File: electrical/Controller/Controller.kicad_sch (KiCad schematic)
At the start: 49 parts, among them J1 USB4105-GF-A, J2 UART, J3 SWD, J4 TC2030-NL, J5 I2C, SW1 SYS, U1 USBLC6-2P6, U2 LP5912-3.3DRV, U3 W25Q16JVUXIQ, U4 RP2040, U5 ABPMRRV001PD2A3, Y1 ABM8-272-T3

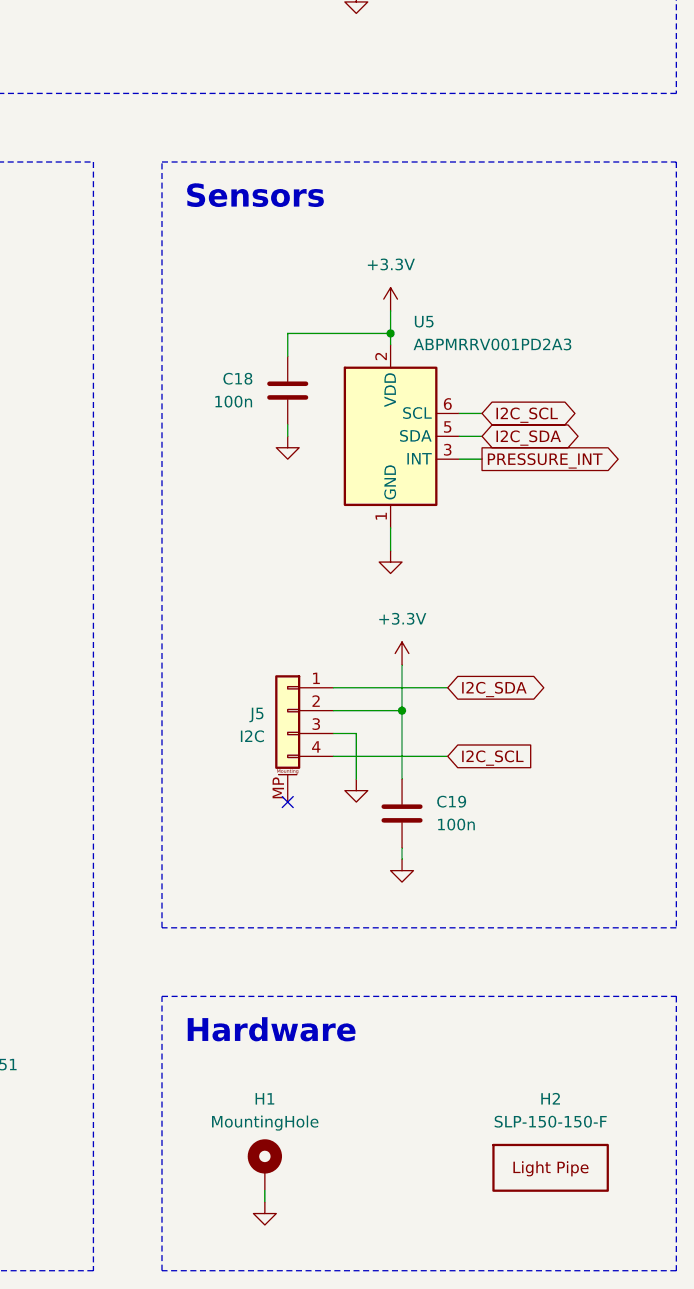
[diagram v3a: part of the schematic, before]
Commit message: Use 5-pin connector for I2C
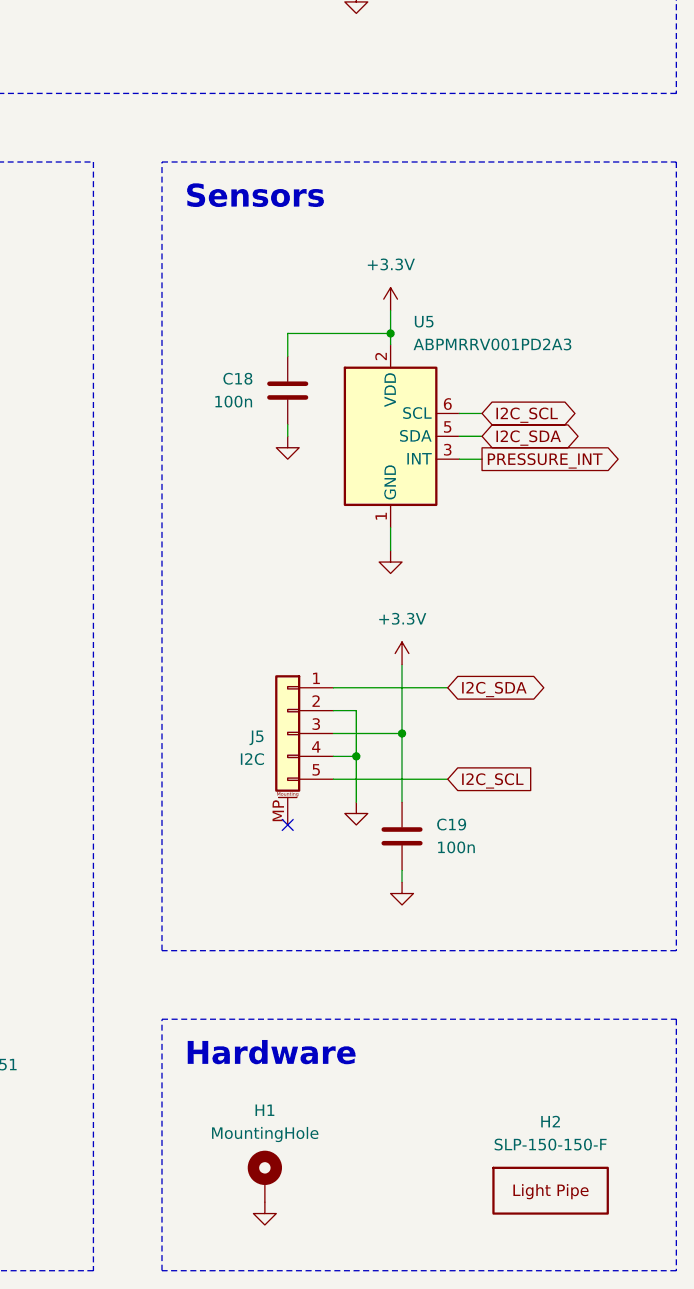
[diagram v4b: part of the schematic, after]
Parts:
- J5: footprint Connector_Molex:Molex_PicoBlade_53261-0471_1x04-1MP_P1.25mm_Horizontal -> Connector_Molex:Molex_PicoBlade_53261-0571_1x05-1MP_P1.25mm_Horizontal; symbol Connector_Generic_MountingPin:Conn_01x04_MountingPin -> Connector_Generic_MountingPin:Conn_01x05_MountingPin; LCSC C5119769 -> C392176
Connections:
- net +3.3V: now also J5.3 (Pin_3); no longer J5.2 (Pin_2)
- net GND: now also J5.2 (Pin_2), J5.4 (Pin_4); no longer J5.3 (Pin_3)
- net I2C_SCL: now also J5.5 (Pin_5); no longer J5.4 (Pin_4)
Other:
- moved on the sheet: C19, H1, H2
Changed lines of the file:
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@@
 	)
 	(rectangle
-		(start 331.47 193.04)
+		(start 331.47 195.58)
 		(end 388.62 223.52)
 		(stroke
@@
 	(rectangle
 		(start 331.47 100.33)
-		(end 388.62 185.42)
+		(end 388.62 187.96)
 		(stroke
 			(width 0)
@@
 	(text "Hardware"
 		(exclude_from_sim no)
-		(at 334.01 195.58 0)
+		(at 334.01 198.12 0)
 		(effects
 			(font
@@
 	)
 	(junction
+		(at 353.06 166.37)
+		(diameter 0)
+		(color 0 0 0 0)
+	)
+	(junction
 		(at 78.74 158.75)
 		(diameter 0)
@@
 	)
 	(junction
-		(at 358.14 161.29)
+		(at 358.14 163.83)
 		(diameter 0)
 		(color 0 0 0 0)
@@
 	)
 	(no_connect
-		(at 345.44 171.45)
+		(at 345.44 173.99)
 	)
 	(no_connect
@@
 	(wire
 		(pts
+			(xy 353.06 161.29) (xy 353.06 166.37)
+		)
+		(stroke
+			(width 0)
+			(type default)
+		)
+	)
+	(wire
+		(pts
 			(xy 88.9 152.4) (xy 91.44 152.4)
 		)
@@
 	(wire
 		(pts
-			(xy 350.52 166.37) (xy 363.22 166.37)
+			(xy 350.52 168.91) (xy 363.22 168.91)
 		)
 		(stroke
@@
 	(wire
 		(pts
-			(xy 353.06 163.83) (xy 353.06 168.91)
+			(xy 353.06 166.37) (xy 353.06 171.45)
 		)
 		(stroke
@@
 	(wire
 		(pts
-			(xy 358.14 168.91) (xy 358.14 161.29)
+			(xy 358.14 171.45) (xy 358.14 163.83)
 		)
 		(stroke
@@
 	(wire
 		(pts
-			(xy 350.52 163.83) (xy 353.06 163.83)
+			(xy 350.52 166.37) (xy 353.06 166.37)
 		)
 		(stroke
@@
 	(wire
 		(pts
-			(xy 358.14 161.29) (xy 358.14 156.21)
+			(xy 358.14 163.83) (xy 358.14 156.21)
 		)
 		(stroke
@@
 	(wire
 		(pts
-			(xy 350.52 161.29) (xy 358.14 161.29)
+			(xy 350.52 163.83) (xy 358.14 163.83)
 		)
 		(stroke
@@
 	(wire
 		(pts
-			(xy 77.47 67.31) (xy 77.47 69.85)
+			(xy 350.52 161.29) (xy 353.06 161.29)
 		)
 		(stroke
@@
 	(wire
 		(pts
-			(xy 264.16 69.85) (xy 264.16 72.39)
+			(xy 77.47 67.31) (xy 77.47 69.85)
 		)
 		(stroke
@@
 	(wire
 		(pts
-			(xy 342.9 215.9) (xy 342.9 214.63)
+			(xy 264.16 69.85) (xy 264.16 72.39)
 		)
 		(stroke
@@
 	(wire
 		(pts
-			(xy 358.14 177.8) (xy 358.14 176.53)
+			(xy 358.14 180.34) (xy 358.14 179.07)
 		)
 		(stroke
@@
 	(global_label "I2C_SCL"
 		(shape input)
-		(at 363.22 166.37 0)
+		(at 363.22 168.91 0)
 		(fields_autoplaced yes)
 		(effects
@@
 		)
 		(property "Intersheetrefs" "${INTERSHEET_REFS}"
-			(at 373.7647 166.37 0)
+			(at 373.7647 168.91 0)
 			(effects
 				(font
@@
 	(symbol
 		(lib_id "power:GND")
-		(at 358.14 177.8 0)
+		(at 358.14 180.34 0)
 		(unit 1)
 		(exclude_from_sim no)
@@
 		(fields_autoplaced yes)
 		(property "Reference" "#PWR0147"
-			(at 358.14 184.15 0)
+			(at 358.14 186.69 0)
 			(effects
 				(font
@@
 		)
 		(property "Value" "GND"
-			(at 358.14 182.88 0)
+			(at 358.14 185.42 0)
 			(effects
 				(font
@@
 		)
 		(property "Footprint" ""
-			(at 358.14 177.8 0)
+			(at 358.14 180.34 0)
 			(effects
 				(font
@@
 		)
 		(property "Datasheet" ""
-			(at 358.14 177.8 0)
+			(at 358.14 180.34 0)
 			(effects
 				(font
@@
 		)
 		(property "Description" "Power symbol creates a global label with name \"GND\" , ground"
-			(at 358.14 177.8 0)
+			(at 358.14 180.34 0)
 			(effects
 				(font
@@
 	(symbol
 		(lib_id "Device:C")
-		(at 358.14 172.72 0)
+		(at 358.14 175.26 0)
 		(unit 1)
 		(exclude_from_sim no)
@@
 		(dnp no)
 		(property "Reference" "C19"
-			(at 361.95 171.4499 0)
+			(at 361.95 173.9899 0)
 			(effects
 				(font
@@
 		)
 		(property "Value" "100n"
-			(at 361.95 173.9899 0)
+			(at 361.95 176.5299 0)
 			(effects
 				(font
@@
 		)
 		(property "Footprint" "Capacitor_SMD:C_0402_1005Metric"
-			(at 359.1052 176.53 0)
+			(at 359.1052 179.07 0)
 			(effects
 				(font
@@
 		)
 		(property "Datasheet" "~"
-			(at 358.14 172.72 0)
+			(at 358.14 175.26 0)
 			(effects
 				(font
@@
 		)
 		(property "Description" "Unpolarized capacitor"
-			(at 358.14 172.72 0)
+			(at 358.14 175.26 0)
 			(effects
 				(font
@@
 		)
 		(property "LCSC" "C1525"
-			(at 358.14 172.72 0)
+			(at 358.14 175.26 0)
 			(effects
 				(font
@@
 	)
 	(symbol
-		(lib_id "Connector_Generic_MountingPin:Conn_01x04_MountingPin")
-		(at 345.44 161.29 0)
+		(lib_id "Connector_Generic_MountingPin:Conn_01x05_MountingPin")
+		(at 345.44 163.83 0)
 		(mirror y)
 		(unit 1)
@@
 		(dnp no)
 		(property "Reference" "J5"
-			(at 342.9 161.6455 0)
+			(at 342.9 164.1855 0)
 			(effects
 				(font
@@
 		)
 		(property "Value" "I2C"
-			(at 342.9 164.1855 0)
+			(at 342.9 166.7255 0)
 			(effects
 				(font
@@
 			)
 		)
-		(property "Footprint" "Connector_Molex:Molex_PicoBlade_53261-0471_1x04-1MP_P1.25mm_Horizontal"
-			(at 345.44 161.29 0)
+		(property "Footprint" "Connector_Molex:Molex_PicoBlade_53261-0571_1x05-1MP_P1.25mm_Horizontal"
+			(at 345.44 163.83 0)
 			(effects
 				(font
@@
 			)
 		)
-		(property "Datasheet" "https://www.jst-mfg.com/product/pdf/eng/eSH.pdf"
-			(at 345.44 161.29 0)
+		(property "Datasheet" "https://www.molex.com/content/dam/molex/molex-dot-com/products/automated/en-us/salesdrawingpdf/532/53261/532610571_sd.pdf?inline"
+			(at 345.44 163.83 0)
 			(effects
 				(font
@@
 			)
 		)
-		(property "Description" "Molex 0532610471"
-			(at 345.44 161.29 0)
+		(property "Description" "Molex 0532610571"
+			(at 345.44 163.83 0)
 			(effects
 				(font
@@
 			)
 		)
-		(property "LCSC" "C5119769"
-			(at 345.44 161.29 0)
+		(property "LCSC" "C392176"
+			(at 345.44 163.83 0)
 			(effects
 				(font
@@
 		(pin "4"
 		)
+		(pin "5"
+		)
 		(instances
 			(project ""
@@
 	(symbol
 		(lib_id "power:GND")
-		(at 353.06 168.91 0)
+		(at 353.06 171.45 0)
 		(mirror y)
 		(unit 1)
@@
 		(fields_autoplaced yes)
 		(property "Reference" "#PWR0102"
-			(at 353.06 175.26 0)
+			(at 353.06 177.8 0)
 			(effects
 				(font
@@
 		)
 		(property "Value" "GND"
-			(at 353.06 173.99 0)
+			(at 353.06 176.53 0)
 			(effects
 				(font
@@
 		)
 		(property "Footprint" ""
-			(at 353.06 168.91 0)
+			(at 353.06 171.45 0)
 			(effects
 				(font
@@
 		)
 		(property "Datasheet" ""
-			(at 353.06 168.91 0)
+			(at 353.06 171.45 0)
 			(effects
 				(font
@@
 		)
 		(property "Description" "Power symbol creates a global label with name \"GND\" , ground"
-			(at 353.06 168.91 0)
+			(at 353.06 171.45 0)
 			(effects
 				(font
@@
 	(symbol
 		(lib_id "Mechanical:MountingHole_Pad")
-		(at 342.9 212.09 0)
+		(at 342.9 213.36 0)
 		(unit 1)
 		(exclude_from_sim no)
@@
 		(dnp no)
 		(property "Reference" "H1"
-			(at 342.9 204.47 0)
+			(at 342.9 205.74 0)
 			(effects
 				(font
@@
 		)
 		(property "Value" "MountingHole"
-			(at 342.9 207.01 0)
+			(at 342.9 208.28 0)
 			(effects
 				(font
@@
 		)
 		(property "Footprint" "MountingHole:MountingHole_3.2mm_M3_Pad"
-			(at 342.9 212.09 0)
+			(at 342.9 213.36 0)
 			(effects
 				(font
@@
 		)
 		(property "Datasheet" "~"
-			(at 342.9 212.09 0)
+			(at 342.9 213.36 0)
 			(effects
 				(font
@@
 		)
 		(property "Description" "Mounting Hole with connection"
-			(at 342.9 212.09 0)
+			(at 342.9 213.36 0)
 			(effects
 				(font
@@
 	(symbol
 		(lib_id "MidiConcertina:LightPipe")
-		(at 374.65 212.09 0)
+		(at 374.65 214.63 0)
 		(unit 1)
 		(exclude_from_sim no)
@@
 		(dnp no)
 		(property "Reference" "H2"
-			(at 374.65 204.47 0)
+			(at 374.65 207.01 0)
 			(effects
 				(font
@@
 		)
 		(property "Value" "SLP-150-150-F"
-			(at 374.65 207.01 0)
+			(at 374.65 209.55 0)
 			(effects
 				(font
@@
 		)
 		(property "Footprint" "MidiConcertina:Bivar_SLP3-150-150-F"
-			(at 374.65 212.09 0)
+			(at 374.65 214.63 0)
 			(effects
 				(font
@@
 		)
 		(property "Datasheet" "https://www.bivar.com/parts_content/Datasheets/SLP3-150-XXX-X.pdf"
-			(at 374.65 212.09 0)
+			(at 374.65 214.63 0)
 			(effects
 				(font
@@
 		)
 		(property "Description" ""
-			(at 374.65 212.09 0)
+			(at 374.65 214.63 0)
 			(effects
 				(font
@@
 		)
 		(property "LCSC" ""
-			(at 374.65 212.09 0)
+			(at 374.65 214.63 0)
 			(effects
 				(font

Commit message: More work on controller design
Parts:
- removed D2: ESD351, Diode_SMD:D_0402_1005Metric, symbol Device:D_Zener
- C1, C10, C11, C12, C15, C18, C19, C4, C5, C6, C7, C8, C9: Part (none) -> Samsung CL05B104KO5NNNC
- C13, C14, C2, C3: Part (none) -> Samsung CL05A105KA5NQNC
- C16, C17: Part (none) -> Fenghua 0402CG150J500NT
- D1: Part (none) -> KENTO KT-0603R
- D2: renamed from D3; Part (none) -> TI ESD351DPYR
- H2: value SLP-150-150-F -> SLP3-150-150-F; now left out of the parts list
- J1: Part (none) -> G-Switch GT-USB-7010ASV
- J2: value UART -> ~; Label (none) -> UART; Part (none) -> JST SM03B-SRSS-TB
- J3: value SWD -> ~; Label (none) -> SWD; Part (none) -> JST SM03B-SRSS-TB
- J5: value I2C -> ~; footprint Connector_Molex:Molex_PicoBlade_53261-0571_1x05-1MP_P1.25mm_Horizontal -> Connector_Molex:Molex_PicoBlade_53261-0671_1x06-1MP_P1.25mm_Horizontal; symbol Connector_Generic_MountingPin:Conn_01x05_MountingPin -> Connector_Generic_MountingPin:Conn_01x06_MountingPin; LCSC C392176 -> C99277; Label (none) -> I2C; Part (none) -> Molex 532610671
- R1, R2: Part (none) -> UNI-ROYAL 0402WGF5101TCE
- R10, R11, R3: Part (none) -> UNI-ROYAL 0402WGF1001TCE
- R12, R13, R8, R9: Part (none) -> UNI-ROYAL 0402WGF1000TCE
- R4, R5: Part (none) -> UNI-ROYAL 0402WGF270JTCE
- R6, R7: Part (none) -> UNI-ROYAL 0402WGF2201TCE
- SW1: value SYS -> ~; Label (none) -> SYS; Part (none) -> Panasonic EVQPUL02K
- U1: Part (none) -> ST USBLC6-2P6
- U2: Part (none) -> TI LP5912-3.3DRVR
- U3: Part (none) -> Winbond W25Q16JVUXIQ
- U4: Part (none) -> Raspberry Pi RP2040
- U5: Part (none) -> Honeywell ABPMRRV001PD2A3
- Y1: value ABM8-272-T3 -> 12 MHz; Part (none) -> Abracon ABM8-272-T3
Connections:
- net GND: now also J5.6 (Pin_6)
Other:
- moved on the sheet: C19, D2, SW1

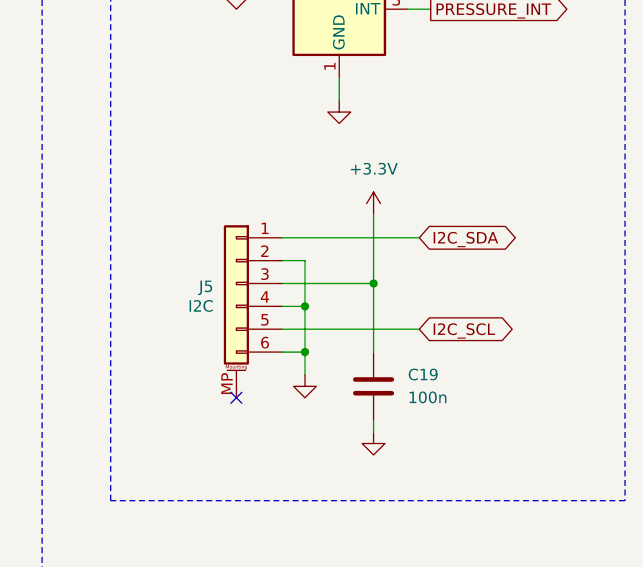
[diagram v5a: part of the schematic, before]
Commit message: Adjust I2C layout
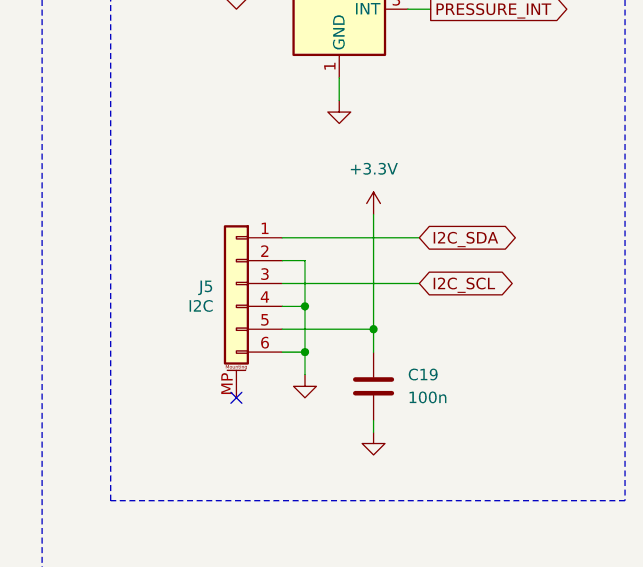
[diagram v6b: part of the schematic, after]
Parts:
- R6, R7: footprint Resistor_SMD:R_0402_1005Metric -> Resistor_SMD:R_0603_1608Metric; LCSC C25879 -> C4190; Part UNI-ROYAL 0402WGF2201TCE -> UNI-ROYAL 0603WAF2201T5E
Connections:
- net +3.3V: now also J5.5 (Pin_5); no longer J5.3 (Pin_3)
- net I2C_SCL: now also J5.3 (Pin_3); no longer J5.5 (Pin_5)
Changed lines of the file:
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@@
 	)
 	(junction
+		(at 360.68 168.91)
+		(diameter 0)
+		(color 0 0 0 0)
+	)
+	(junction
 		(at 278.13 158.75)
 		(diameter 0)
@@
 	)
 	(junction
-		(at 360.68 163.83)
-		(diameter 0)
-		(color 0 0 0 0)
-	)
-	(junction
 		(at 264.16 82.55)
 		(diameter 0)
@@
 	(wire
 		(pts
-			(xy 350.52 168.91) (xy 365.76 168.91)
+			(xy 350.52 163.83) (xy 365.76 163.83)
 		)
 		(stroke
@@
 	(wire
 		(pts
-			(xy 360.68 171.45) (xy 360.68 163.83)
+			(xy 360.68 171.45) (xy 360.68 168.91)
 		)
 		(stroke
@@
 	(wire
 		(pts
-			(xy 360.68 163.83) (xy 360.68 156.21)
+			(xy 360.68 156.21) (xy 360.68 168.91)
 		)
 		(stroke
@@
 	(wire
 		(pts
-			(xy 350.52 163.83) (xy 360.68 163.83)
+			(xy 350.52 168.91) (xy 360.68 168.91)
 		)
 		(stroke
@@
 	(global_label "I2C_SCL"
 		(shape bidirectional)
-		(at 365.76 168.91 0)
+		(at 365.76 163.83 0)
 		(fields_autoplaced yes)
 		(effects
@@
 		)
 		(property "Intersheetrefs" "${INTERSHEET_REFS}"
-			(at 377.416 168.91 0)
+			(at 377.416 163.83 0)
 			(effects
 				(font
@@
 			)
 		)
-		(property "Footprint" "Resistor_SMD:R_0402_1005Metric"
+		(property "Footprint" "Resistor_SMD:R_0603_1608Metric"
 			(at 268.986 147.574 90)
 			(effects
@@
 			)
 		)
-		(property "Datasheet" "https://www.lcsc.com/datasheet/lcsc_datasheet_2411221126_UNI-ROYAL-Uniroyal-Elec-0402WGF2201TCE_C25879.pdf"
+		(property "Datasheet" "https://www.lcsc.com/datasheet/lcsc_datasheet_2411221126_UNI-ROYAL-Uniroyal-Elec-0603WAF2201T5E_C4190.pdf"
 			(at 267.97 147.32 0)
 			(effects
@@
 			)
 		)
-		(property "Description" "62.5mW 50V ±1% 2.2kΩ Resistor, ROHS"
+		(property "Description" "100mW 75V ±1% 2.2kΩ Resistor, ROHS"
 			(at 267.97 147.32 0)
 			(effects
@@
 			)
 		)
-		(property "LCSC" "C25879"
+		(property "LCSC" "C4190"
 			(at 267.97 147.32 0)
 			(effects
@@
 			)
 		)
-		(property "Part" "UNI-ROYAL 0402WGF2201TCE"
+		(property "Part" "UNI-ROYAL 0603WAF2201T5E"
 			(at 267.97 147.32 0)
 			(effects
@@
 			)
 		)
-		(property "Footprint" "Resistor_SMD:R_0402_1005Metric"
+		(property "Footprint" "Resistor_SMD:R_0603_1608Metric"
 			(at 279.146 147.574 90)
 			(effects
@@
 			)
 		)
-		(property "Datasheet" "https://www.lcsc.com/datasheet/lcsc_datasheet_2411221126_UNI-ROYAL-Uniroyal-Elec-0402WGF2201TCE_C25879.pdf"
+		(property "Datasheet" "https://www.lcsc.com/datasheet/lcsc_datasheet_2411221126_UNI-ROYAL-Uniroyal-Elec-0603WAF2201T5E_C4190.pdf"
 			(at 278.13 147.32 0)
 			(effects
@@
 			)
 		)
-		(property "Description" "62.5mW 50V ±1% 2.2kΩ Resistor, ROHS"
+		(property "Description" "100mW 75V ±1% 2.2kΩ Resistor, ROHS"
 			(at 278.13 147.32 0)
 			(effects
@@
 			)
 		)
-		(property "LCSC" "C25879"
+		(property "LCSC" "C4190"
 			(at 278.13 147.32 0)
 			(effects
@@
 			)
 		)
-		(property "Part" "UNI-ROYAL 0402WGF2201TCE"
+		(property "Part" "UNI-ROYAL 0603WAF2201T5E"
 			(at 278.13 147.32 0)
 			(effects
